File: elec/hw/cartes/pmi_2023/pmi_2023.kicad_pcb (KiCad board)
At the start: 2 copper layers, 149.3 x 73 mm, 285 parts, among them J1 con_servo, J10 Conn_01x01_Pin, J11 Conn_01x01_Socket, J12 Conn_01x01_Pin, J13 Conn_01x01_Pin, J14 Conn_01x01_Socket, J15 Conn_01x01_Socket, J16 Conn_01x01_Pin, J17 Conn_01x01_Pin, J19 Conn_01x01_Pin, J2 con_servo, J20 Conn_01x01_Socket, J21 Conn_01x01_Socket, J22 Conn_01x01_Socket, J23 Conn_01x01_Pin, J24 Conn_01x01_Pin, J27 Conn_01x01_Socket, J28 Conn_01x01_Socket, J29 Conn_01x01_Socket, J3 con_servo, J30 Conn_01x01_Socket, J31 Conn_01x01_Pin, J33 Conn_01x01_Socket, J34 Conn_01x01_Socket, J35 Conn_01x01_Pin, J36 Conn_01x01_Socket, J37 Conn_01x01_Pin, J38 Conn_01x01_Socket, J4 con_servo, J41 Conn_01x01_Socket, J42 Conn_01x01_Socket, J43 Conn_01x01_Socket, J44 Conn_01x01_Pin, J45 Conn_01x01_Socket, J46 Conn_01x01_Pin, J5 254, J7 USB4105-GF-A-060, J8 254, J9 Conn_01x01_Socket, Q2 2N7002, Q3 DMP2008UFG-7, SW1 ESE22MH22, SW2 ESE22MH24, SW3 MSS12C02LS-BB2.0, SW5 DS1040-04RN, SW6 2425755-1, SW7 MSS12C02LS-BB2.0, SW8 MSS12C02LS-BB2.0, U1 DRV8231ADDAR, U10 tof_sensor_master, U11 XRA1200PIG16TR-F, U12 LSM6DSO32XTR, U13 GP2S60B, U14 GP2S60B, U15 GP2S60B, U16 GP2S60B, U17 tof_sensor_master, U18 EESX1321, U19 GP2S60B, U2 DRV8231ADDAR, U20 GP2S60B, U21 tof_sensor_master, U23 PCA9685PW, U24 SN74LVC1T45DBV, U25 SN74LVC1T45DBV, U26 SN74LVC1T45DBV, U27 SN74LVC1T45DBV, U28 TLV61070A, U29 TLV61070A, U3 EESX1321, U32 ESP32-S3-WROOM-1, U33 TLV61070A, U34 TLV61070A, U35 LDL1117S33R, U4 EESX1321, U5 AD8531ARTZ, U6 tof_sensor_master, U7 XRA1200PIG16TR-F, U8 GP2S60B, U9 GP2S60B

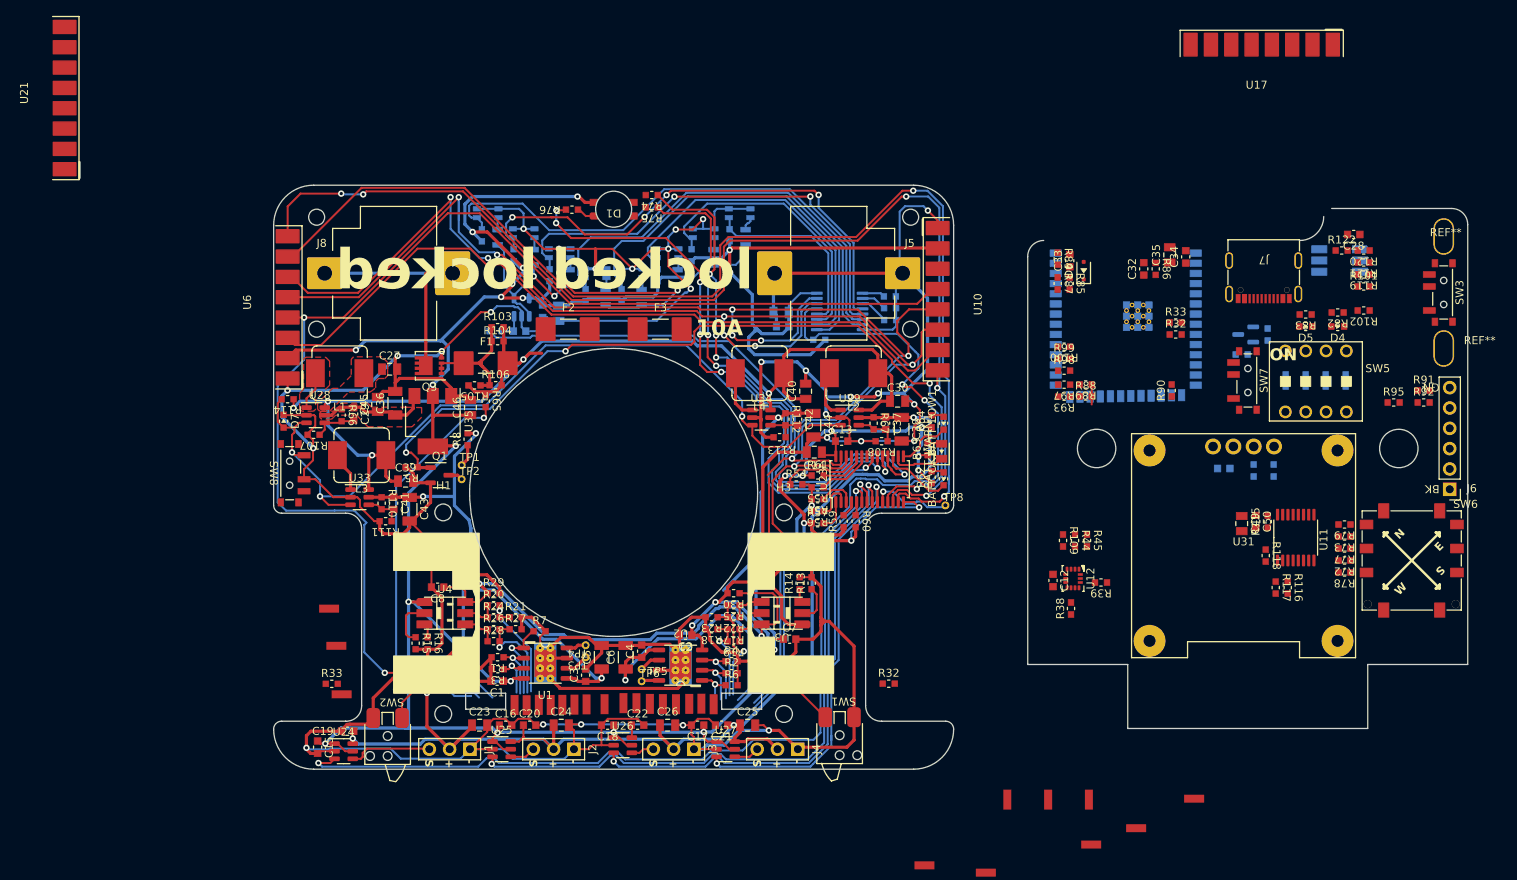
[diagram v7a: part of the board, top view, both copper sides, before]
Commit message: front and back tof added, selector changed, ready to route
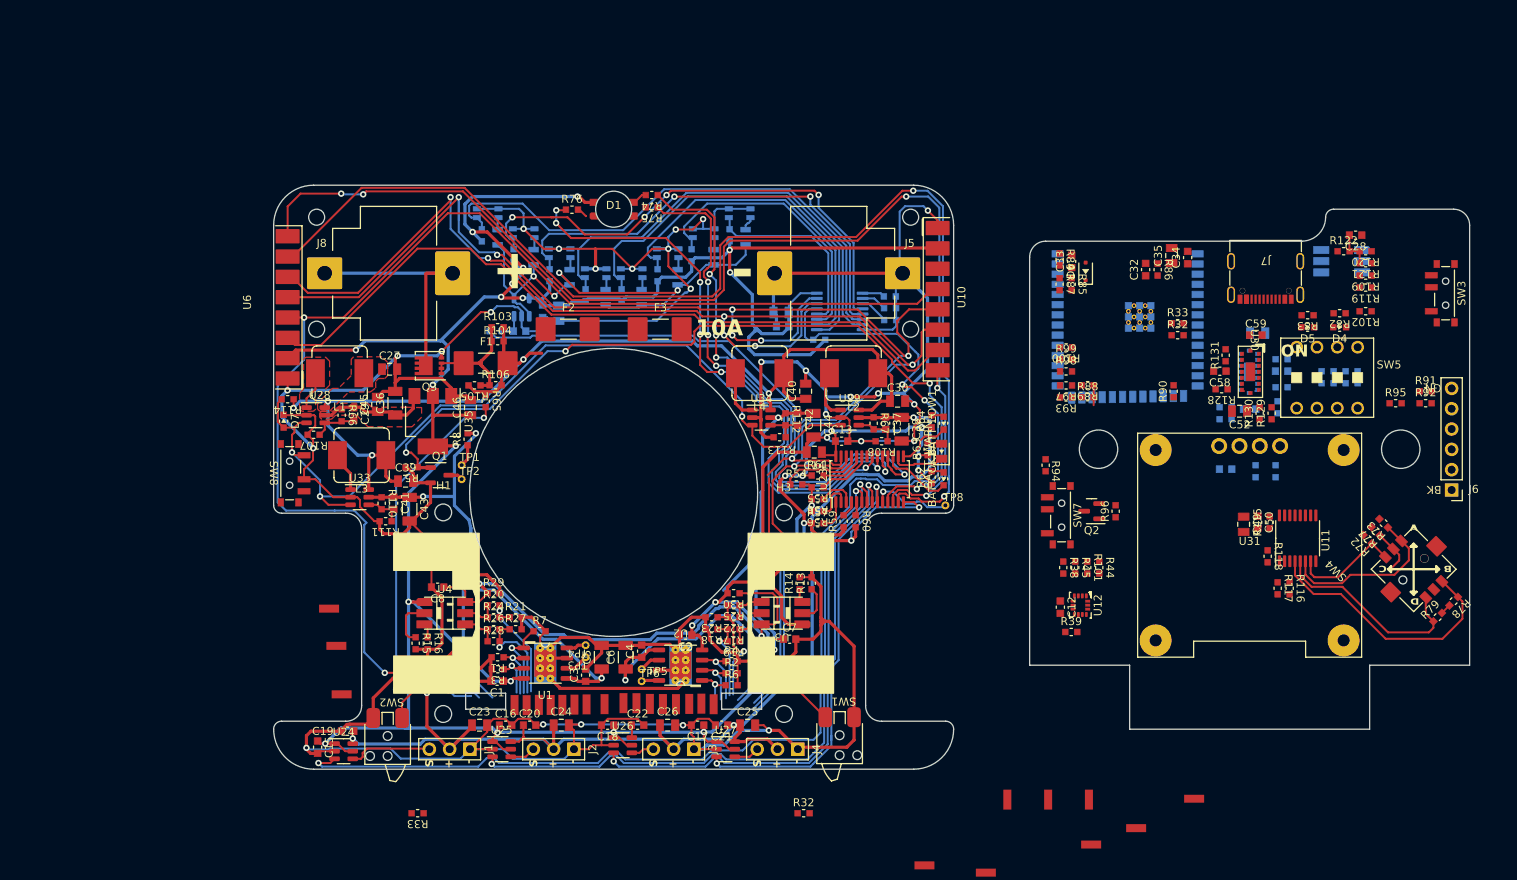
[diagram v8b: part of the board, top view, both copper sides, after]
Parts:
- removed REF** (x2): oblong_2mmx3.5mm, cocotter_others:oblong_2mmx3.5mm
- removed SW6: 2425755-1, cocotter_connectors:2425755-1
- removed U17, U21: tof_sensor_master, cocotter_connectors:tof_sensor_male
- added C51: 10µF 16V, cocotter_capacitors:C_0805_2012Metric, B.Cu at (223.0, 98.5)
- added C52: 10µF 16V, cocotter_capacitors:C_0805_2012Metric, F.Cu at (220.8, 108.2)
- added C53: 100nF 50V, cocotter_capacitors:C_0603_1608Metric, B.Cu at (222.0, 108.0)
- added C57: 100nF 50V, cocotter_capacitors:C_0603_1608Metric, B.Cu at (226.0, 103.2)
- added C58: 100nF 50V, cocotter_capacitors:C_0603_1608Metric, F.Cu at (218.3, 103.2)
- added C59: 100nF 50V, cocotter_capacitors:C_0603_1608Metric, F.Cu at (222.8, 98.8)
- added R123: 10k, cocotter_resistor:r0603_reflow, B.Cu at (226.0, 105.2)
- added R124: 10k, cocotter_resistor:r0603_reflow, B.Cu at (225.5, 107.8)
- added R125: 100k, cocotter_resistor:r0603_reflow, B.Cu at (219.8, 108.5)
- added R126: 100k, cocotter_resistor:r0603_reflow, B.Cu at (218.2, 108.5)
- added R127: 100k, cocotter_resistor:r0603_reflow, B.Cu at (226.0, 101.8)
- added R128: 10k, cocotter_resistor:r0603_reflow, F.Cu at (218.5, 105.5)
- added R129: 100k, cocotter_resistor:r0603_reflow, F.Cu at (224.8, 108.5)
- added R130: 100k, cocotter_resistor:r0603_reflow, F.Cu at (223.2, 108.5)
- added R131: 100k, cocotter_resistor:r0603_reflow, F.Cu at (219.0, 101.2)
- added SW4: 2425755-1, cocotter_connectors:TM-4175-B-A, F.Cu at (242.5, 128.0)
- added U22: VL53L5CXV0GC, cocotter_ic:VL53L5CX, B.Cu at (222.0, 101.0)
- added U30: VL53L5CXV0GC, cocotter_ic:VL53L5CX, F.Cu at (222.0, 101.0)
- Q2, R94, R96: moved to F.Cu
- moved R109 50.3 mm to (236.5, 91.3), turned to 180 degrees
- moved R101 49.3 mm to (201.7, 127.8), turned to -90 degrees
- moved Q2 29.3 mm to (202.2, 120.8)
- moved R96 29.1 mm to (205.2, 120.8), turned to 90 degrees
- moved SW7 28.7 mm to (198.5, 121.2)
- moved R94 28.1 mm to (196.5, 115.0), turned to -90 degrees
- moved R33 19.4 mm to (118.0, 158.5), turned to 180 degrees
- moved R32 19.4 mm to (166.2, 158.5)
- moved R79 16.4 mm to (245.5, 134.0), turned to 45 degrees
- moved R78 14.1 mm to (247.5, 132.0), turned to -135 degrees
- moved R39 7.22 mm to (199.7, 135.8), turned to 0 degrees
- moved R38 5.20 mm to (198.7, 127.8), turned to -90 degrees
- moved R73 5.16 mm to (238.8, 122.2), turned to 135 degrees
- moved R44 4.55 mm to (203.2, 127.8)
- moved R68 4.51 mm to (231.0, 104.0)
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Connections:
- net /actuators/LED_RGB_W_3v3 renamed /actuators/u23_unused_led15
- BATT_LOW1 pad A: Net-(BATT_LOW1-PadA) -> (no net)
- BATT_LOW1 pad C: /actuators/led_vbatt_error -> (no net)
- C28 pad 1: +3V3 -> +3V3_m
- J38 pad 1: /sensors/tof_irq -> /boards interface/tof_irq
- R119 pad 1: +3V3 -> +3V3_m
- R119 pad 2: /boards interface/interface/emergency_stop_3v3 -> /boards interface/com/emergency_stop_3v3
- R122 pad 1: /boards interface/interface/start_robot_3v3 -> /boards interface/com/start_robot_3v3
- R38 pad 2: Net-(U12-INT1) -> /boards interface/Sensor module/gyro_irq_3v3
- R64 pad 2: Net-(BATT_LOW1-PadA) -> Net-(BATT_LOW1-A)
- R74 pad 1: /LED_RGB_R_3v3 -> /actuators/led_RGB_r_3v3
- R75 pad 1: /LED_RGB_B_3v3 -> /actuators/led_RGB_b_3v3
- R76 pad 1: /LED_RGB_G_3v3 -> /actuators/led_RGB_g_3v3
- SW3 pad B: /boards interface/interface/emergency_stop_3v3 -> /boards interface/com/emergency_stop_3v3
- U10 pad 3: /sensors/enable_tof2 -> unconnected-(U10-enable_next_board_3v3-Pad3)
- U10 pad 4: /sensors/tof_irq -> unconnected-(U10-detect_irq_3v3-Pad4)
- U11 pad 10: /boards interface/interface/select1 -> /boards interface/interface/conf2
- U11 pad 11: /boards interface/interface/select2 -> /boards interface/interface/conf1
- U11 pad 12: /boards interface/interface/select3 -> /boards interface/interface/conf0
- U11 pad 4: /boards interface/interface/conf0 -> /boards interface/interface/select3
- U11 pad 5: /boards interface/interface/conf1 -> /boards interface/interface/select0
- U11 pad 6: /boards interface/interface/conf2 -> /boards interface/interface/select1
- U11 pad 7: /boards interface/interface/conf3 -> /boards interface/interface/select2
- U11 pad 9: /boards interface/interface/select0 -> /boards interface/interface/conf3
- U12 pad 12: /boards interface/Sensor module/gyro_ncs_3v3 -> /boards interface/Sensor module/gyro_mosi_3v3
- U12 pad 14: /boards interface/Sensor module/gyro_mosi_3v3 -> (no net)
- U12 pad 4: Net-(U12-INT1) -> /boards interface/Sensor module/gyro_irq_3v3
- U18 pad 1: +3V3 -> +3V3_m
- U18 pad 5: /boards interface/interface/start_robot_3v3 -> /boards interface/com/start_robot_3v3
- U18 pad 6: +3V3 -> +3V3_m
- U23 pad 19: /actuators/LED_RGB_R_3v3 -> /actuators/led_RGB_r_3v3
- U23 pad 20: /actuators/LED_RGB_G_3v3 -> /actuators/led_RGB_g_3v3
- U23 pad 21: /actuators/LED_RGB_B_3v3 -> /actuators/led_RGB_b_3v3
- U31 pad 1: GND_M -> (no net)
- U32 pad 22: unconnected-(U32-IO14,RTC_GPIO14,GPIO14,TOUCH14,FSPIWP,FSPIDQS,SUBSPIWP-Pad22) -> /boards interface/Sensor module/gyro_irq_3v3
- U32 pad 23: unconnected-(U32-IO21,RTC_GPIO21,GPIO21-Pad23) -> /boards interface/com/emergency_stop_3v3
- U32 pad 28: unconnected-(U32-IO35,SPIIO6,GPIO35,FSPID,SUBSPID-Pad28) -> /boards interface/com/start_robot_3v3
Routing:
- net (no net): track 30.0 -> 168.0 mm, vias 1 -> 11
- net /actuators/LED_RGB_B_3v3: track 73.6 -> 0.00 mm, vias 6 -> 0
- net /actuators/led_RGB_r_3v3: track 0.00 -> 67.1 mm, vias 0 -> 4
- net /actuators/LED_RGB_R_3v3: track 67.1 -> 0.00 mm, vias 4 -> 0
- net /actuators/LED_RGB_G_3v3: track 64.4 -> 0.00 mm, vias 4 -> 0
- net /boards interface/interface/select3: track 0.00 -> 32.8 mm
- net /boards interface/interface/select0: track 0.00 -> 25.8 mm
- net /boards interface/interface/select1: track 0.00 -> 21.4 mm
- net /boards interface/interface/select2: track 0.00 -> 13.8 mm
- net /boards interface/interface/select4: track 0.00 -> 5.25 mm
- net GND: track 695.5 -> 700.3 mm
- net Net-(D1-C_BLUE): track 2.18 -> 0.00 mm
- net Net-(D1-C_RED): track 0.00 -> 1.78 mm
- net Net-(BATT_LOW1-PadA): track 1.58 -> 0.00 mm
- net Net-(BATT_LOW1-A): track 0.00 -> 1.58 mm
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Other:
- board size 149.3 x 73 mm -> 149.5 x 73 mm
- board text added: "+"
- board text added: "-"
- board text removed: "locked"
